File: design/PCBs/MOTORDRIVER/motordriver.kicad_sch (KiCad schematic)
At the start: 0 parts

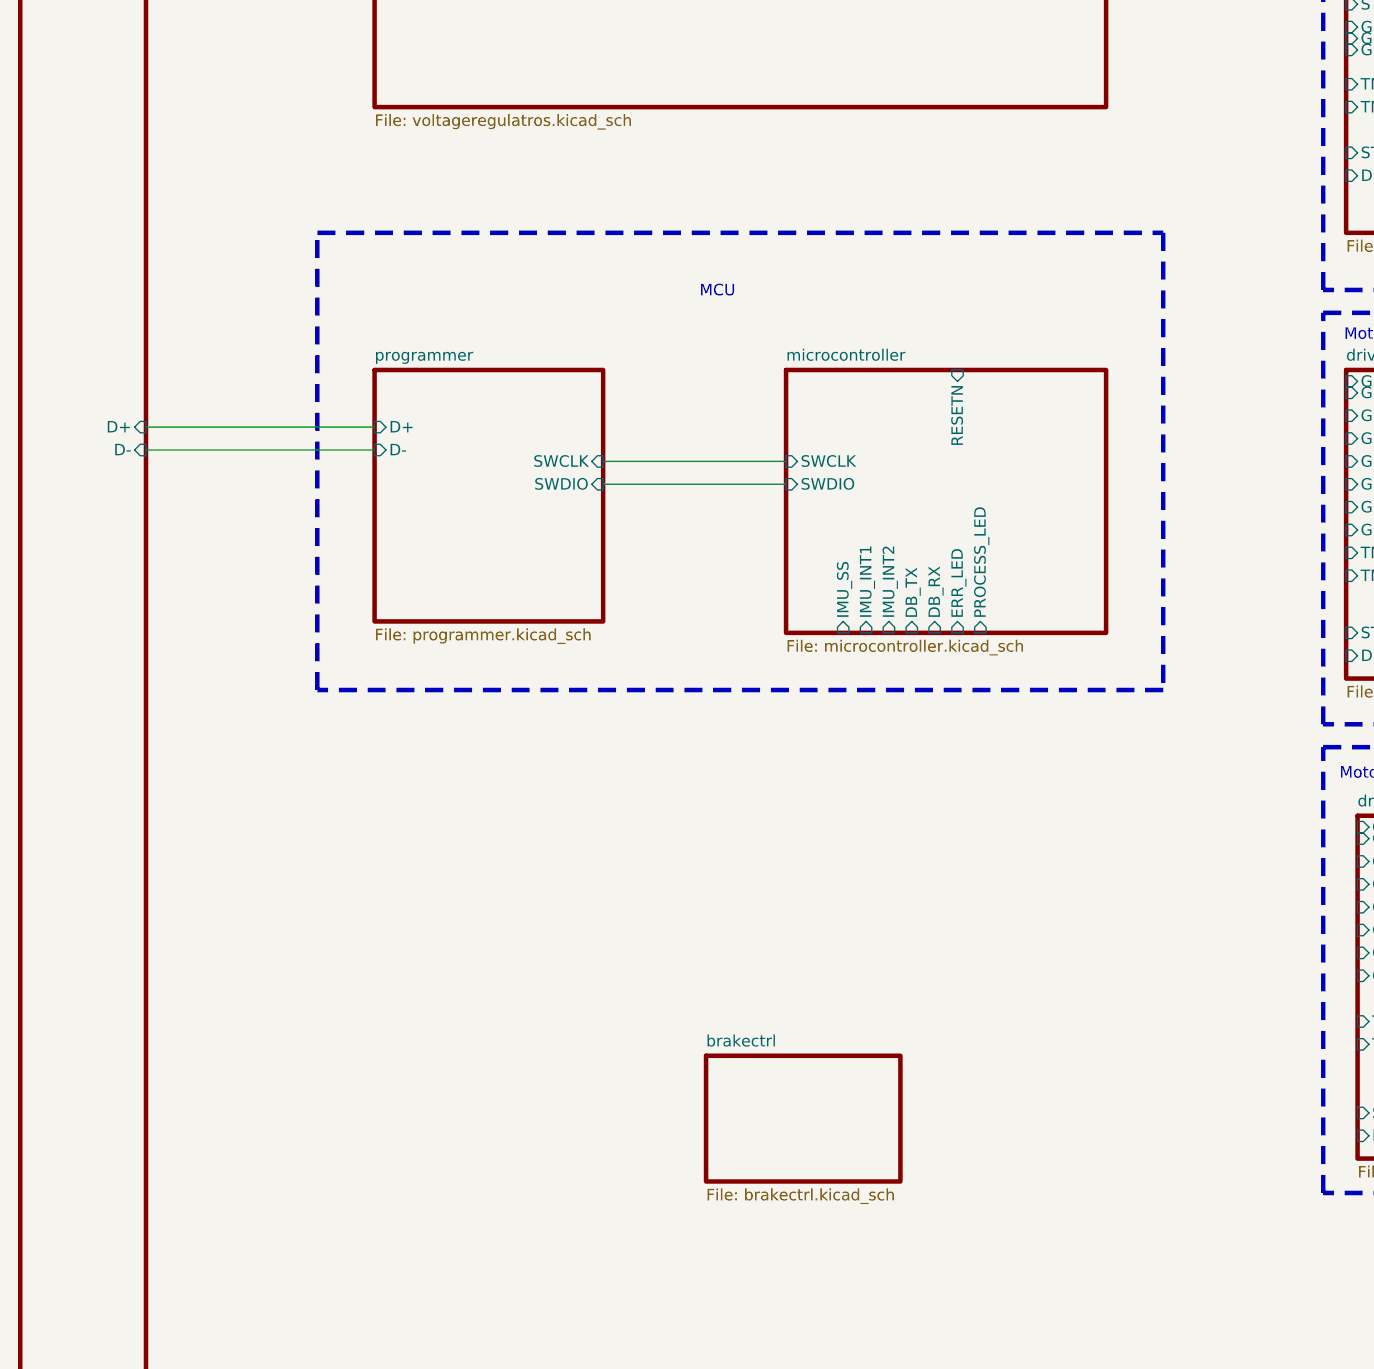
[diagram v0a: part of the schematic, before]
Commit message: Added micro-servo headers Added header for FFC cable IMU PCB
We need to set IMU PCB input to correspond to
the one we have made here.
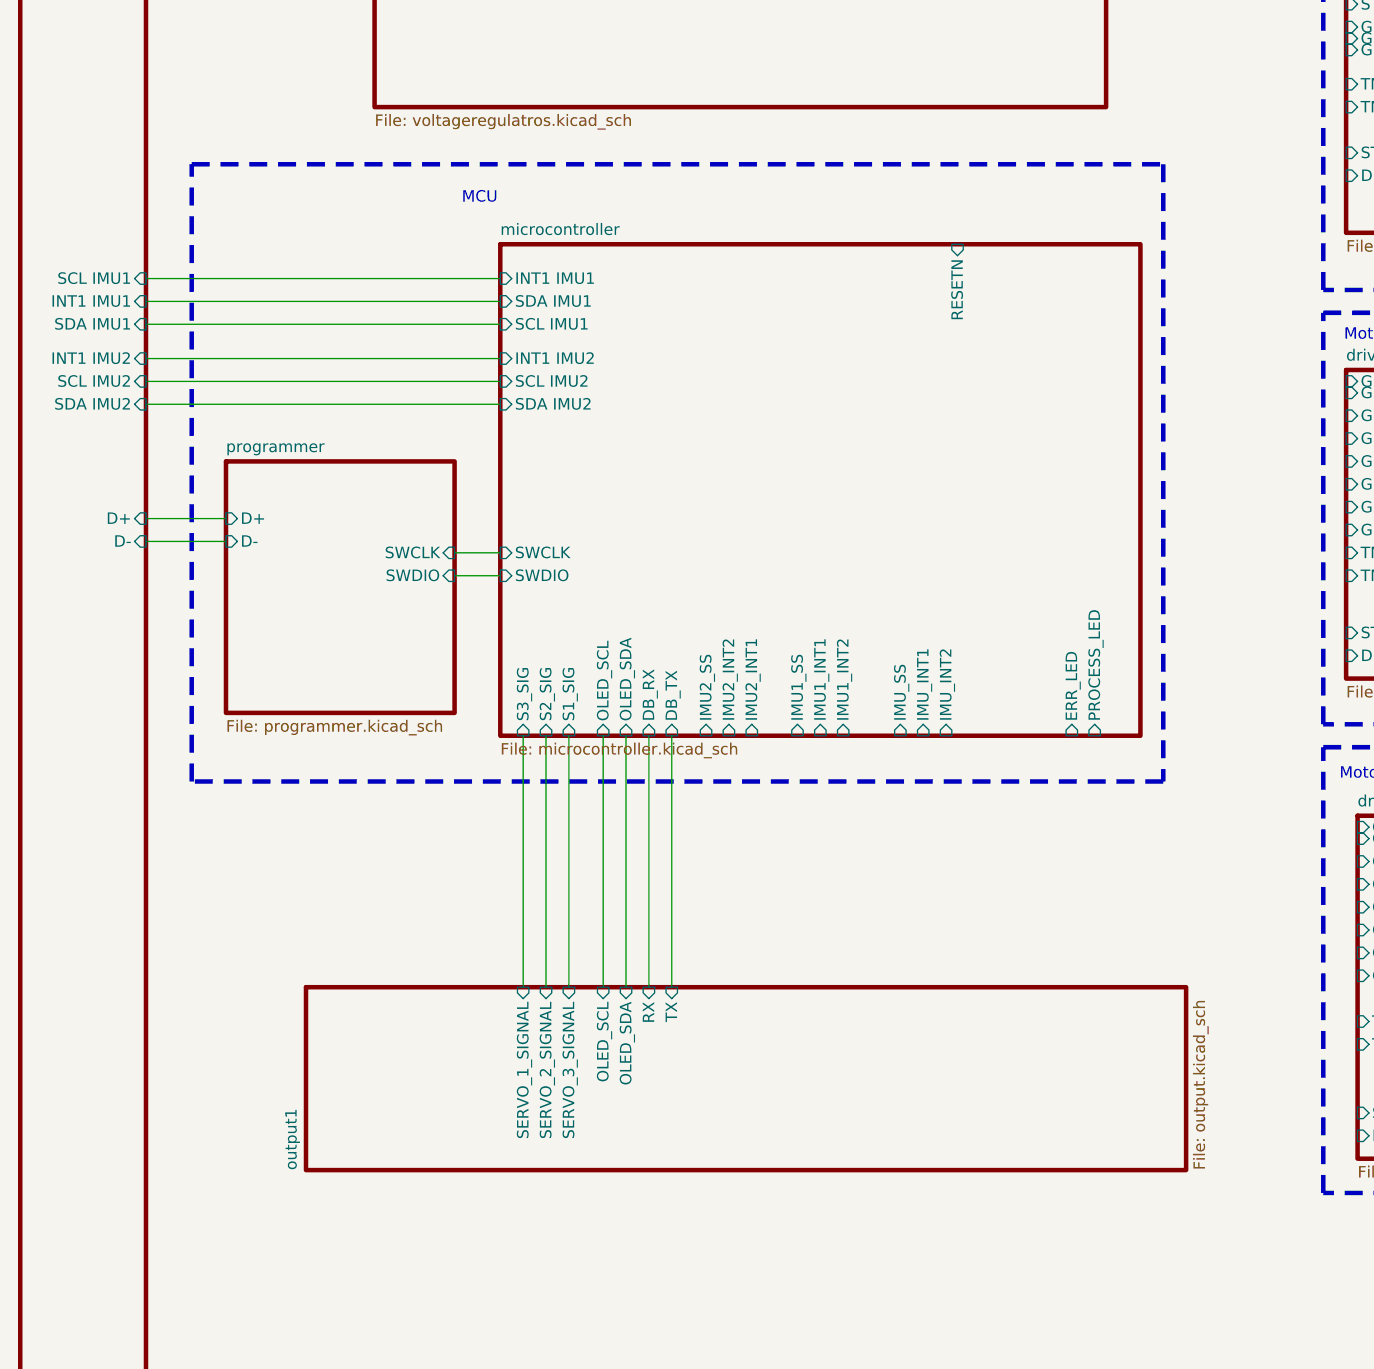
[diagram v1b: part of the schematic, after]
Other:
- removed sheet brakectrl
- added sheet output1 (output.kicad_sch)
- sheet input ports: added INT1 IMU1, INT1 IMU2, SCL IMU1, SCL IMU2, SDA IMU1, SDA IMU2; removed none
- sheet microcontroller ports: added IMU1_INT1, IMU1_INT2, IMU1_SS, IMU2_INT1, IMU2_INT2, IMU2_SS, INT1 IMU1, INT1 IMU2, OLED_SCL, OLED_SDA, S1_SIG, S2_SIG, S3_SIG, SCL IMU1, SCL IMU2, SDA IMU1, SDA IMU2; removed none

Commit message: drivergates IC coupled up
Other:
- sheet microcontroller ports: added none; removed IMU1_INT1, IMU1_INT2, IMU1_SS, IMU2_INT1, IMU2_INT2, IMU2_SS, IMU_INT1, IMU_INT2, IMU_SS
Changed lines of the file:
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@@
 	)
 	(sheet
-		(at 50.8 139.7)
-		(size 97.79 20.32)
+		(at 72.39 139.7)
+		(size 54.61 20.32)
 		(fields_autoplaced yes)
 		(stroke
@@
 		)
 		(property "Sheetname" "output1"
-			(at 49.9146 160.02 90)
+			(at 71.5046 160.02 90)
 			(effects
 				(font
@@
 		)
 		(property "Sheetfile" "output.kicad_sch"
-			(at 149.3484 160.02 90)
+			(at 127.7584 160.02 90)
 			(effects
 				(font
@@
 			)
 		)
-		(pin "IMU_SS" input
-			(at 116.84 111.76 270)
-			(effects
-				(font
-					(size 1.27 1.27)
-				)
-				(justify left)
-			)
-		)
-		(pin "IMU_INT1" input
-			(at 119.38 111.76 270)
-			(effects
-				(font
-					(size 1.27 1.27)
-				)
-				(justify left)
-			)
-		)
-		(pin "IMU_INT2" input
-			(at 121.92 111.76 270)
-			(effects
-				(font
-					(size 1.27 1.27)
-				)
-				(justify left)
-			)
-		)
 		(pin "DB_TX" input
 			(at 91.44 111.76 270)
@@
 			)
 		)
-		(pin "IMU2_INT1" input
-			(at 100.33 111.76 270)
-			(effects
-				(font
-					(size 1.27 1.27)
-				)
-				(justify left)
-			)
-		)
-		(pin "IMU2_INT2" input
-			(at 97.79 111.76 270)
-			(effects
-				(font
-					(size 1.27 1.27)
-				)
-				(justify left)
-			)
-		)
-		(pin "IMU2_SS" input
-			(at 95.25 111.76 270)
-			(effects
-				(font
-					(size 1.27 1.27)
-				)
-				(justify left)
-			)
-		)
 		(pin "OLED_SCL" input
 			(at 83.82 111.76 270)
@@
 			(effects
 				(font
-					(size 1.27 1.27)
-				)
-				(justify left)
-			)
-		)
-		(pin "IMU1_SS" input
-			(at 105.41 111.76 270)
-			(effects
-				(font
-					(size 1.27 1.27)
-				)
-				(justify left)
-			)
-		)
-		(pin "IMU1_INT1" input
-			(at 107.95 111.76 270)
-			(effects
-				(font
-					(size 1.27 1.27)
-				)
-				(justify left)
-			)
-		)
-		(pin "IMU1_INT2" input
-			(at 110.49 111.76 270)
-			(effects
-				(font

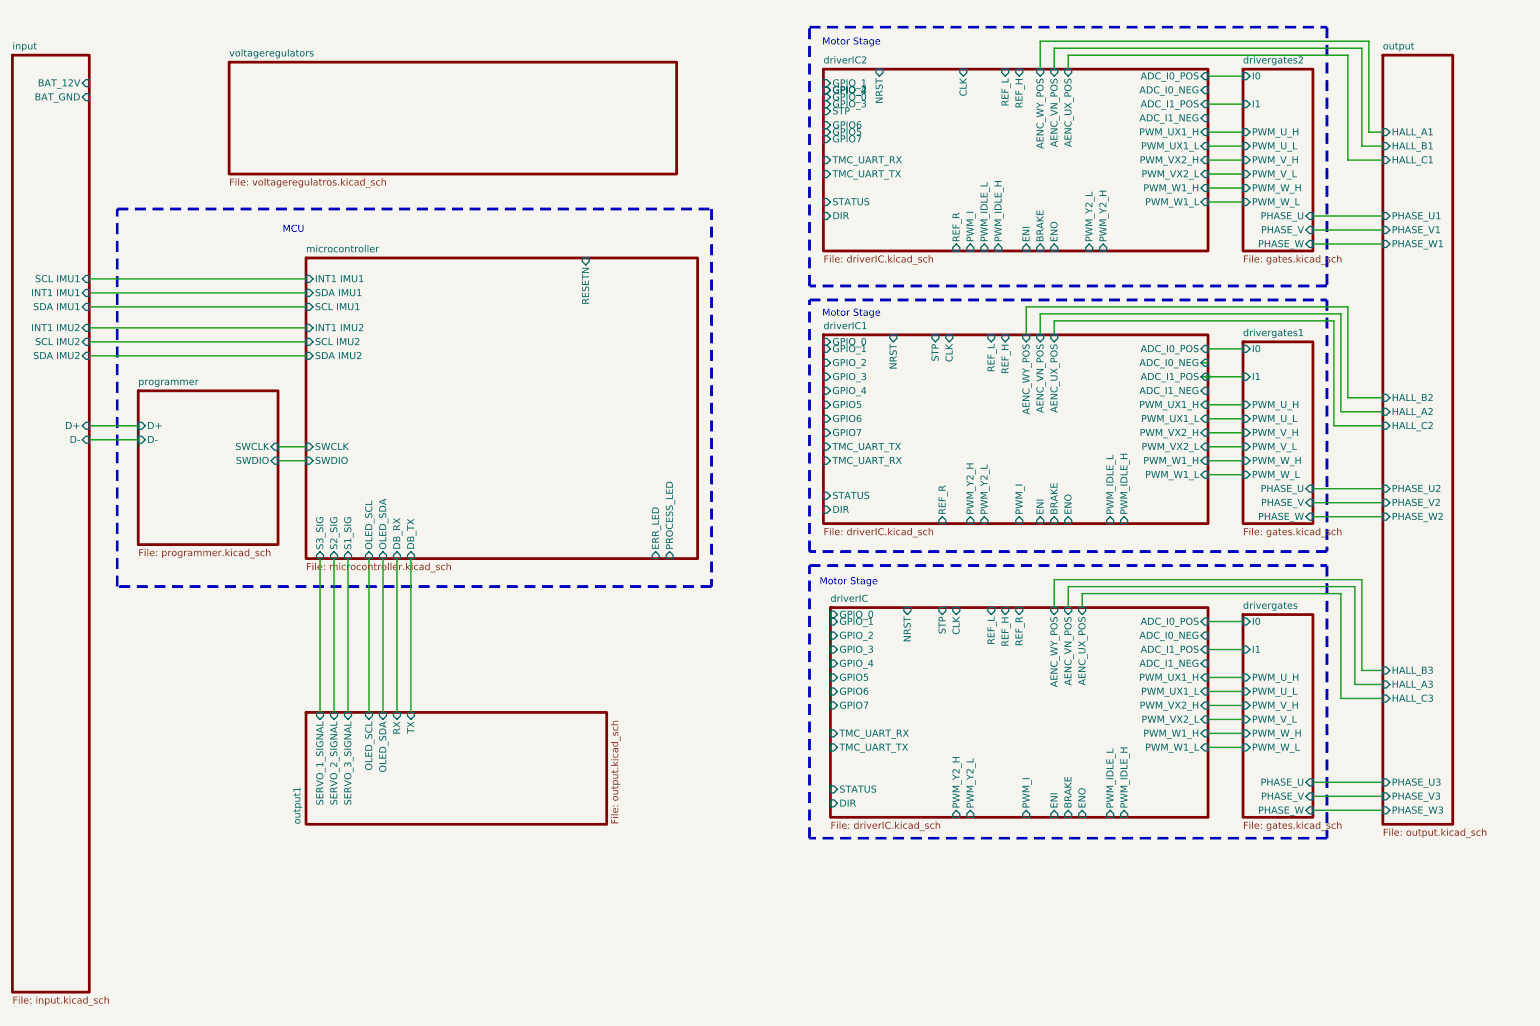
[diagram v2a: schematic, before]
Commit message: worked on power and merged programmer and microcontroller sheets
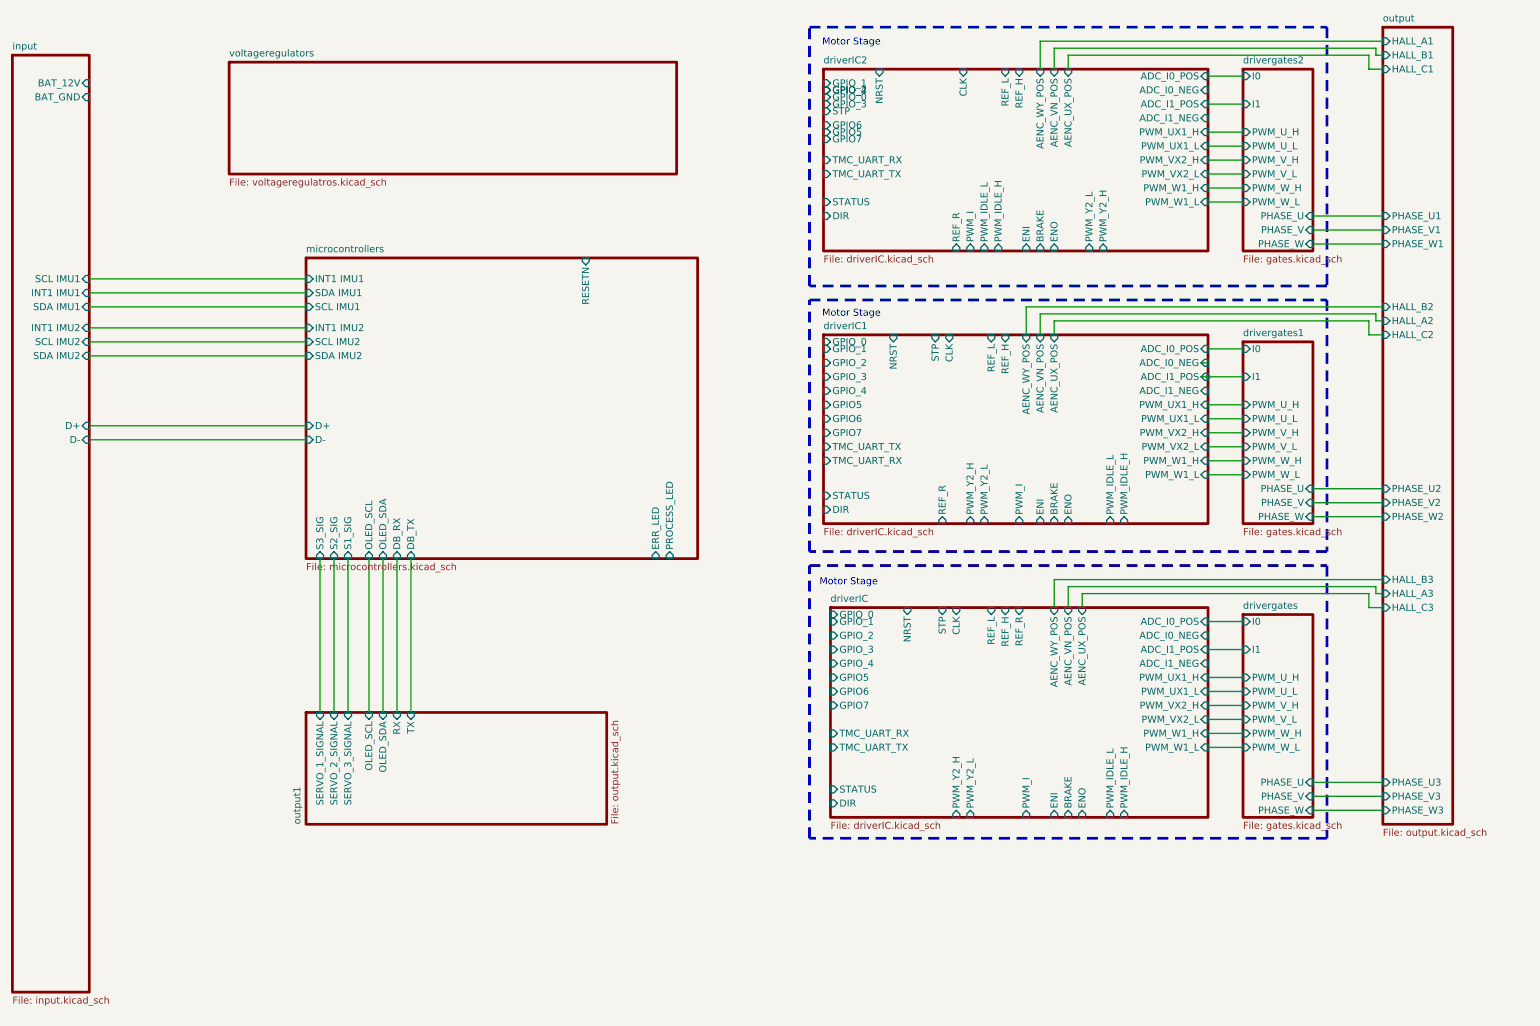
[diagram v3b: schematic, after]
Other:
- sheet microcontroller renamed microcontrollers
- removed sheet programmer
- sheet microcontrollers: file microcontroller.kicad_sch -> microcontrollers.kicad_sch
- sheet microcontrollers ports: added D+, D-; removed SWCLK, SWDIO
- note removed: "MCU"

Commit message: finished 12v voltage, The components for alost all ICs need values. Cleaned up a bit
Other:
- sheet drivergates1 ports: added I0_NEG, I0_POS, I1_NEG, I1_POS; removed I0, I1
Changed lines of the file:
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@@
 	(generator_version "8.0")
 	(paper "A4")
-	(junction
-		(at 236.22 78.74)
-		(diameter 0)
-		(color 0 0 0 0)
-	)
-	(wire
-		(pts
-			(xy 236.22 76.2) (xy 234.95 76.2)
-		)
-		(stroke
-			(width 0)
-			(type default)
-		)
-	)
 	(wire
 		(pts
@@
 	(wire
 		(pts
+			(xy 236.22 81.28) (xy 242.57 81.28)
+		)
+		(stroke
+			(width 0)
+			(type default)
+		)
+	)
+	(wire
+		(pts
 			(xy 236.22 146.05) (xy 242.57 146.05)
 		)
@@
 	(wire
 		(pts
+			(xy 236.22 76.2) (xy 242.57 76.2)
+		)
+		(stroke
+			(width 0)
+			(type default)
+		)
+	)
+	(wire
+		(pts
 			(xy 33.02 72.39) (xy 72.39 72.39)
 		)
@@
 	(wire
 		(pts
-			(xy 234.95 78.74) (xy 236.22 78.74)
-		)
-		(stroke
-			(width 0)
-			(type default)
-		)
-	)
-	(wire
-		(pts
 			(xy 208.28 71.12) (xy 208.28 68.58)
 		)
@@
 			)
 		)
-		(pin "I1" input
-			(at 242.57 78.74 180)
+		(pin "PWM_U_H" input
+			(at 242.57 83.82 180)
 			(effects
 				(font
@@
 			)
 		)
-		(pin "I0" input
-			(at 242.57 73.66 180)
+		(pin "PWM_U_L" input
+			(at 242.57 86.36 180)
 			(effects
 				(font
@@
 			)
 		)
-		(pin "PWM_U_H" input
-			(at 242.57 83.82 180)
+		(pin "PWM_V_H" input
+			(at 242.57 88.9 180)
 			(effects
 				(font
@@
 			)
 		)
-		(pin "PWM_U_L" input
-			(at 242.57 86.36 180)
+		(pin "PWM_V_L" input
+			(at 242.57 91.44 180)
 			(effects
 				(font
@@
 			)
 		)
-		(pin "PWM_V_H" input
-			(at 242.57 88.9 180)
+		(pin "PWM_W_L" input
+			(at 242.57 96.52 180)
 			(effects
 				(font
@@
 			)
 		)
-		(pin "PWM_V_L" input
-			(at 242.57 91.44 180)
+		(pin "PWM_W_H" input
+			(at 242.57 93.98 180)
 			(effects
 				(font
@@
 			)
 		)
-		(pin "PWM_W_L" input
-			(at 242.57 96.52 180)
+		(pin "I1_POS" input
+			(at 242.57 78.74 180)
 			(effects
 				(font
@@
 			)
 		)
-		(pin "PWM_W_H" input
-			(at 242.57 93.98 180)
+		(pin "I1_NEG" input
+			(at 242.57 81.28 180)
+			(effects
+				(font
+					(size 1.27 1.27)
+				)
+				(justify left)
+			)
+		)
+		(pin "I0_NEG" input
+			(at 242.57 76.2 180)
+			(effects
+				(font
+					(size 1.27 1.27)
+				)
+				(justify left)
+			)
+		)
+		(pin "I0_POS" input
+			(at 242.57 73.66 180)
 			(effects
 				(font
